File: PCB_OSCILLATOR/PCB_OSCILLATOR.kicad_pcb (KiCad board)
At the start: 2 copper layers, 161.6 x 129 mm, 96 parts, among them J1 Jumper, J10 Jumper, J11 Jumper, J12 Jumper, J13 Jumper, J14 Jumper, J15 Jumper, J16 Jumper, J2 Jumper, J3 Jumper, J4 Jumper, J5 Jumper, J6 Jumper, J7 Jumper, J8 Jumper, J9 Jumper, P1 POWER SUPPLY, P2 SPI_AD5270_1, P3 SPI_AD5270_2, P4 SPI_AD9833_1, P5 SPI_AD9833_2, U1 AD5270, U10 ADR291, U2 AD8421, U3 AD9833, U4 AD5270, U5 AD8421, U6 AD9833, U7 ADG819, U8 ADP3303, U9 AD8651

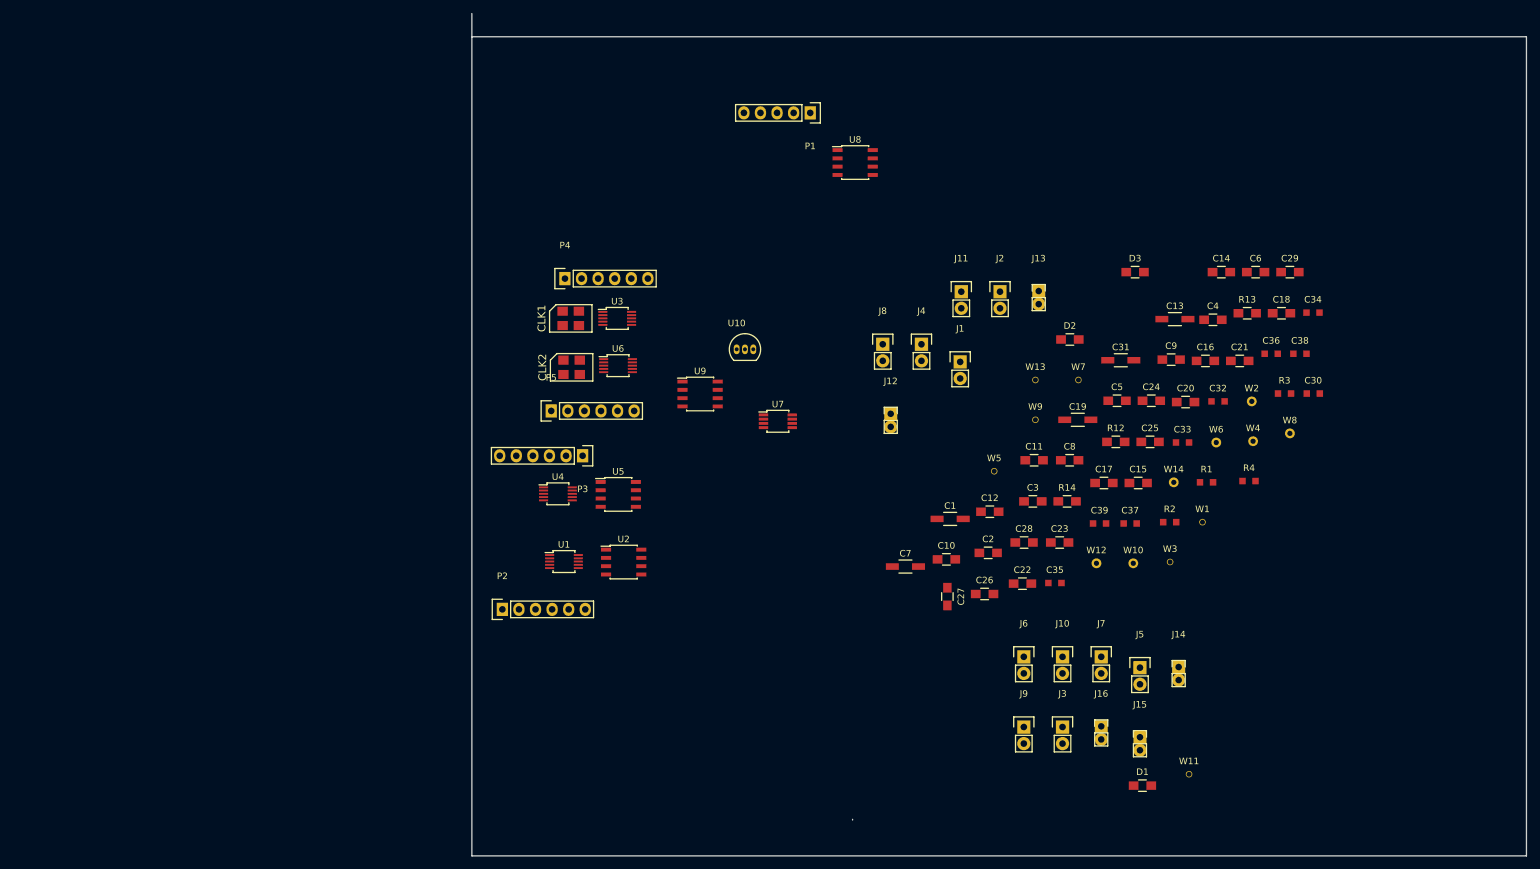
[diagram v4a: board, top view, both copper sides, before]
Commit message: Pequeñas correciones
Cambio de Huellas de capacitores
Correción de footPrint de jumpers con errores
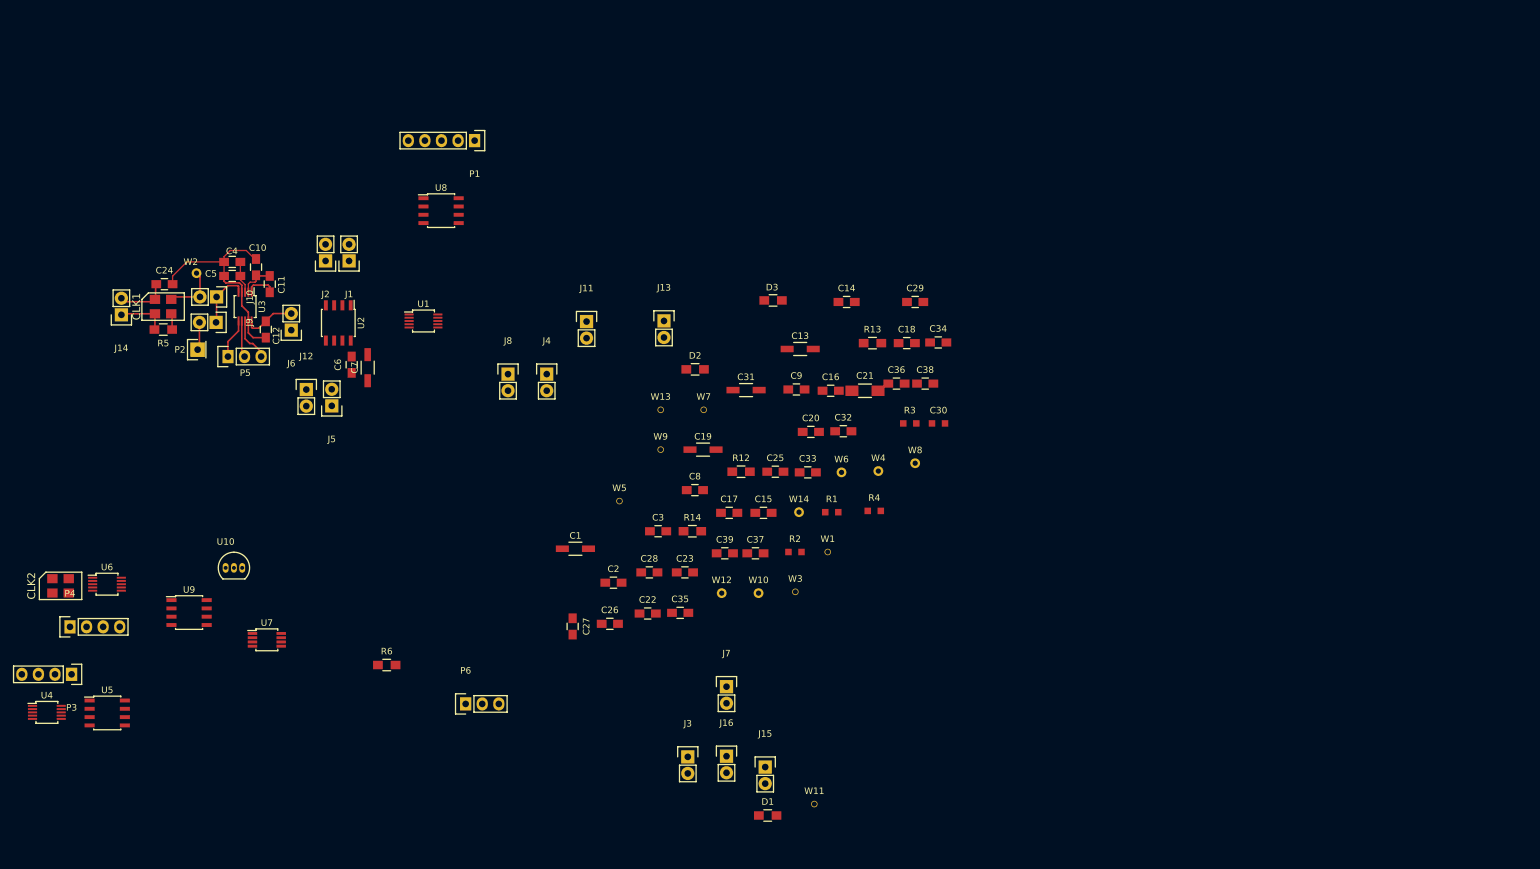
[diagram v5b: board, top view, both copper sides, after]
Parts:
- added P6: SPI_AD9833_2, Socket_Strips:Socket_Strip_Straight_1x03, F.Cu at (119.7, 144.9)
- added R5: 10K, Resistors_SMD:R_0805_HandSoldering, F.Cu at (73.3, 87.6)
- added R6: 10K, Resistors_SMD:R_0805_HandSoldering, F.Cu at (107.6, 139.0)
- C10, C11, C12, C14, C15, C16, C17, C18, C2, C20, C22, C23, C24, C25, C26, C27, C28, C29, C3, C32, C33, C34, C35, C36, C37, C38, C39, C4, C5, C6, C8, C9: footprint Resistors_SMD:R_0805_HandSoldering -> Capacitors_SMD:C_0805_HandSoldering
- C21: footprint Resistors_SMD:R_0805_HandSoldering -> Capacitors_SMD:C_1206_HandSoldering
- P2: value SPI_AD5270_1 -> MCLK_EXTERNAL; footprint Socket_Strips:Socket_Strip_Straight_1x06 -> Socket_Strips:Socket_Strip_Straight_1x01
- P3: value SPI_AD5270_2 -> SPI_AD5270_1; footprint Socket_Strips:Socket_Strip_Straight_1x06 -> Socket_Strips:Socket_Strip_Straight_1x04
- P4: value SPI_AD9833_1 -> SPI_AD5270_2; footprint Socket_Strips:Socket_Strip_Straight_1x06 -> Socket_Strips:Socket_Strip_Straight_1x04
- P5: value SPI_AD9833_2 -> SPI_AD9833_1; footprint Socket_Strips:Socket_Strip_Straight_1x06 -> Socket_Strips:Socket_Strip_Straight_1x03
- moved J14 170.7 mm to (66.9, 85.3), turned to 180 degrees
- moved W2 162.8 mm to (78.4, 78.9)
- moved C24 152.2 mm to (73.5, 80.6)
- moved C4 150.5 mm to (83.9, 77.2), turned to 180 degrees
- moved J10 140.8 mm to (81.5, 82.6), turned to 270 degrees
- moved C6 139.2 mm to (102.2, 93.0), turned to 90 degrees
- moved J9 138.4 mm to (81.4, 86.5), turned to 270 degrees
- moved C5 136.9 mm to (83.9, 79.3), turned to 180 degrees
- moved J5 130.1 mm to (99.2, 99.2), turned to 180 degrees
- moved J6 122.9 mm to (93.0, 87.7), turned to 180 degrees
- moved C11 120.2 mm to (89.7, 80.6), turned to 270 degrees
- moved C10 114.8 mm to (87.5, 78.0), turned to 90 degrees
- moved C12 114.4 mm to (89.0, 87.5), turned to 270 degrees
- moved J2 103.4 mm to (98.2, 77.0), turned to 180 degrees
- moved J1 94.9 mm to (101.8, 77.0), turned to 180 degrees
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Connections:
- J9 pad 2: /MCLK_EXTERNAL -> Net-(J9-Pad2)
- P2 pad 1: /SDO_AD5270_1 -> Net-(J9-Pad2)
- P3 pad 1: /SDO_AD5270_2 -> /SDO_AD5270_1
- P3 pad 2: /DIN_AD5270_2 -> /DIN_AD5270_1
- P3 pad 3: /SCLK_AD5270_2 -> /SCLK_AD5270_1
- P3 pad 4: /_SYNC_AD5270_2 -> /_SYNC_AD5270_1
- P4 pad 1: /SCLK_DDS_1 -> /SDO_AD5270_2
- P4 pad 2: /SDATA_DDS_1 -> /DIN_AD5270_2
- P4 pad 3: /FSYNK_DDS_1 -> /SCLK_AD5270_2
- P4 pad 4: /MCLK_EXTERNAL -> /_SYNC_AD5270_2
- P5 pad 1: /SCLK_DDS_2 -> /SDATA_DDS_1
- P5 pad 2: /SDATA_DDS_2 -> /SCLK_DDS_1
- P5 pad 3: /FSYNK_DDS_2 -> /FSYNK_DDS_1
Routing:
- net /GND: track 0.00 -> 36.4 mm
- net /VDD: track 0.00 -> 13.5 mm
- net Net-(C12-Pad1): track 0.00 -> 9.13 mm
- net Net-(J10-Pad1): track 0.00 -> 8.97 mm
- net /MCLK_DDS_1: track 0.00 -> 8.41 mm
- net Net-(CLK1-Pad1): track 0.00 -> 7.66 mm
- net /FSYNK_DDS_1: track 0.00 -> 6.74 mm
- net /SDATA_DDS_1: track 0.00 -> 6.13 mm
- net /SCLK_DDS_1: track 0.00 -> 5.63 mm
- net Net-(C4-Pad1): track 0.00 -> 4.94 mm
- net Net-(C11-Pad2): track 0.00 -> 4.66 mm
- net Net-(J9-Pad2): track 0.00 -> 4.30 mm
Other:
- board outline removed
- net class Default: clearance 0.2 -> 0.1778; trace_width 0.25 -> 0.1778
- rule trace_clearance: 0.2 -> 0.1778
- rule trace_min: 0.2 -> 0.1524
- rule via_min_size: 0.4 -> 0.5

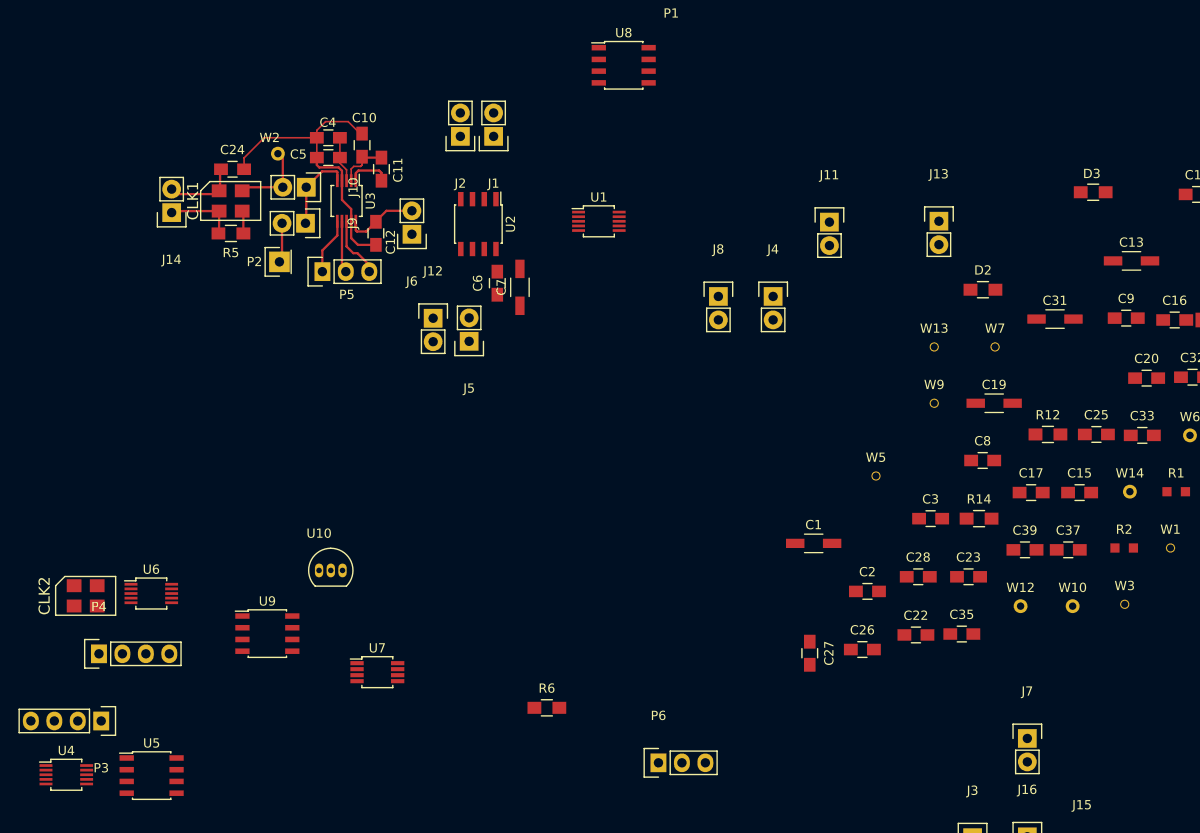
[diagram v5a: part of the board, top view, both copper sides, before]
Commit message: Inicio de borrador de ruteado
//
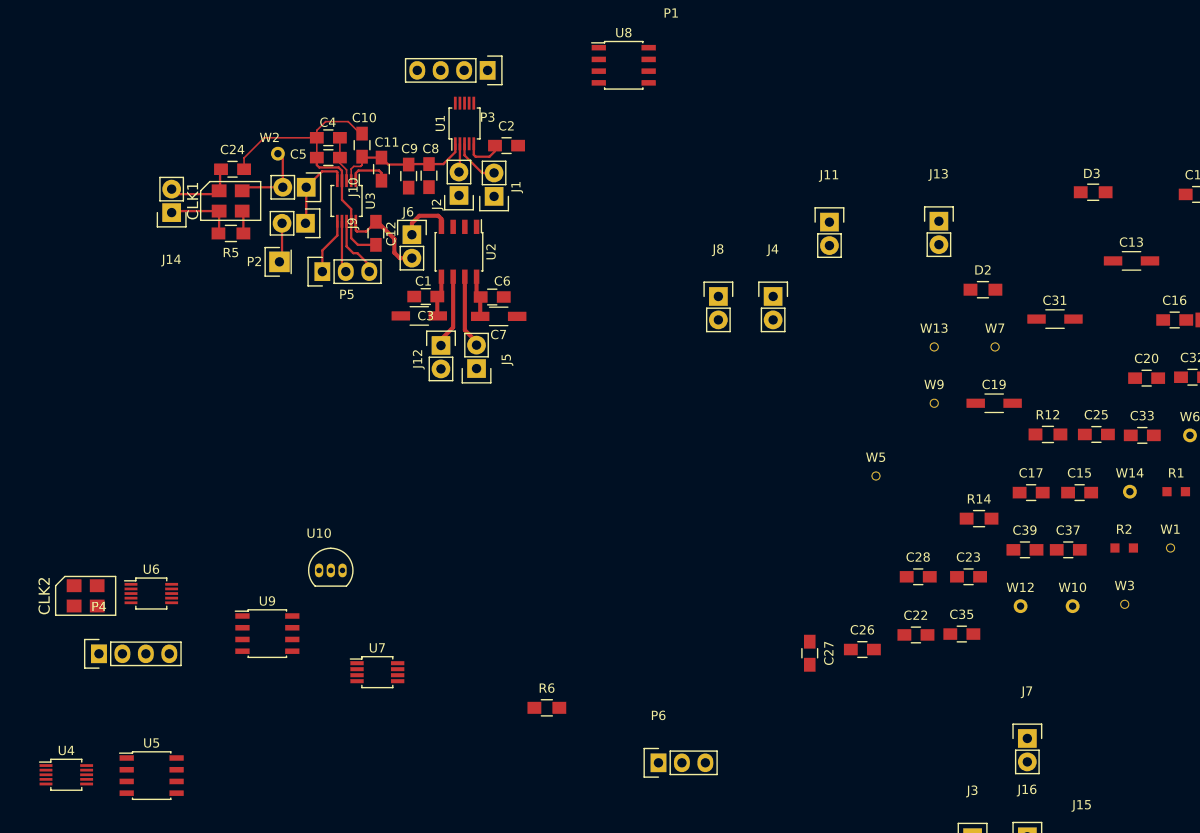
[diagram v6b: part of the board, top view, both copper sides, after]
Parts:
- moved P3 82.0 mm to (101.2, 69.9)
- moved C9 79.2 mm to (92.6, 81.3), turned to 270 degrees
- moved C8 67.5 mm to (94.8, 81.3), turned to 270 degrees
- moved C2 62.1 mm to (103.2, 78.0)
- moved C3 59.7 mm to (94.5, 94.4), turned to 180 degrees
- moved C1 49.3 mm to (93.8, 96.5)
- moved U1 18.0 mm to (98.7, 75.7), turned to 90 degrees
- moved J1 6.50 mm to (101.8, 83.5)
- moved J2 6.40 mm to (98.0, 83.5)
- moved C7 3.90 mm to (102.3, 96.5), turned to 180 degrees
- moved U2 3.66 mm to (98.0, 89.5)
- moved J12 3.07 mm to (96.1, 99.7)
- moved J5 3.06 mm to (100.0, 102.2)
- moved C6 1.60 mm to (101.7, 94.5), turned to 180 degrees
- turned J6 to 0 degrees
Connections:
- U1 pad 2: /A_AD5270_1 -> /W_AD5270_1
- U1 pad 3: /W_AD5270_1 -> /A_AD5270_1
- U4 pad 2: /A_AD5270_2 -> /W_AD5270_2
- U4 pad 3: /W_AD5270_2 -> /A_AD5270_2
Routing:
- net /VDD: track 13.5 -> 23.3 mm
- net Net-(J12-Pad1): track 0.00 -> 7.99 mm
- net Net-(J5-Pad2): track 0.00 -> 7.93 mm
- net /WAVE_DDS_1: track 0.00 -> 5.77 mm
- net /A_AD5270_1: track 0.00 -> 5.73 mm
- net /+12V: track 0.00 -> 4.51 mm
- net /-12V: track 0.00 -> 4.46 mm
- net Net-(C2-Pad1): track 0.00 -> 4.43 mm
- net /W_AD5270_1: track 0.00 -> 3.10 mm
- net Net-(C12-Pad1): track 9.13 -> 11.6 mm
- net /DIN_AD5270_1: track 0.00 -> 0.79 mm

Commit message: Avance pequeño
//
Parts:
- moved C7 6.57 mm to (104.2, 90.2), turned to 270 degrees
- moved C6 3.52 mm to (102.0, 91.0), turned to 270 degrees
- moved J12 3.49 mm to (97.5, 96.5)
- moved J5 3.43 mm to (101.3, 99.0)
- moved C3 1.77 mm to (92.8, 93.7)
- moved C1 1.72 mm to (92.2, 95.8)
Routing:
- net /_SYNC_AD5270_1: track 0.00 -> 6.90 mm
- net /SCLK_AD5270_1: track 0.00 -> 5.23 mm
- net Net-(J1-Pad1): track 0.00 -> 5.23 mm
- net /SDO_AD5270_1: track 0.00 -> 4.93 mm
- net Net-(J2-Pad1): track 0.00 -> 3.66 mm
- net Net-(J12-Pad1): track 7.99 -> 4.41 mm
- net /DIN_AD5270_1: track 0.79 -> 3.62 mm
- net Net-(J5-Pad2): track 7.93 -> 6.13 mm
- net /FSYNK_DDS_1: track 6.74 -> 7.96 mm
- net /-12V: track 4.46 -> 5.44 mm
- net /WAVE_DDS_1: track 5.77 -> 6.64 mm
- net Net-(C12-Pad1): track 11.6 -> 12.4 mm
- net /SCLK_DDS_1: track 5.63 -> 6.22 mm

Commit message: Board al 70%
// =)
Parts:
- moved J15 101.5 mm to (103.2, 74.5), turned to 180 degrees
- moved C34 85.4 mm to (106.6, 90.7), turned to 270 degrees
- moved CLK2 74.6 mm to (109.9, 73.7), turned to 270 degrees
- moved R3 72.3 mm to (116.6, 88.6), turned to 270 degrees
- moved C18 71.5 mm to (117.0, 76.0), turned to 90 degrees
- moved R4 69.3 mm to (116.7, 92.9), turned to 270 degrees
- moved U6 67.2 mm to (112.6, 79.5), turned to 180 degrees
- moved P6 66.7 mm to (107.2, 79.4), turned to 270 degrees
- moved R6 65.1 mm to (106.6, 73.9), turned to 90 degrees
- moved C29 64.8 mm to (139.0, 125.1)
- moved R13 64.8 mm to (132.4, 131.4)
- moved C25 64.5 mm to (113.4, 73.7), turned to 270 degrees
- moved R1 62.9 mm to (119.1, 88.4), turned to 90 degrees
- moved U9 62.4 mm to (124.3, 89.9)
- moved C35 59.4 mm to (108.8, 90.8), turned to 270 degrees
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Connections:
- P6 pad 1: /SCLK_DDS_2 -> /SDATA_DDS_2
- P6 pad 2: /SDATA_DDS_2 -> /SCLK_DDS_2
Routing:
- net /VDD: track 23.3 -> 48.2 mm
- net /REF_0.25V: track 0.00 -> 16.5 mm
- net Net-(R1-Pad1): track 0.00 -> 12.9 mm
- net /FSYNK_DDS_2: track 0.00 -> 7.39 mm
- net Net-(C26-Pad1): track 0.00 -> 7.34 mm
- net /GND: track 36.4 -> 43.6 mm
- net /REF_2.5V: track 0.00 -> 6.77 mm
- net Net-(CLK2-Pad1): track 0.00 -> 6.52 mm
- net Net-(C17-Pad1): track 0.00 -> 6.20 mm
- net /MCLK_DDS_2: track 0.00 -> 6.17 mm
- net Net-(J5-Pad2): track 6.13 -> 0.00 mm
- net /SCLK_DDS_2: track 0.00 -> 5.07 mm
- net /SDATA_DDS_2: track 0.00 -> 3.56 mm
- net /WAVE_DDS_2: track 0.00 -> 3.48 mm
- net Net-(C23-Pad2): track 0.00 -> 2.78 mm
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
